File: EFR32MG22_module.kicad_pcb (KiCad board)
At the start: 2 copper layers, 29.9 x 42 mm, 34 parts, among them J1 USB_B_Micro 10118194-0011LF, J2 Conn_01x10, J3 Conn_ARM_JTAG_SWD_10, J4 Conn_01x10, U1 EFR32MG22C224F512GN32, U2 TLV75533PDBV, Y1 Crystal ECS-384-CDX-1983-TR3

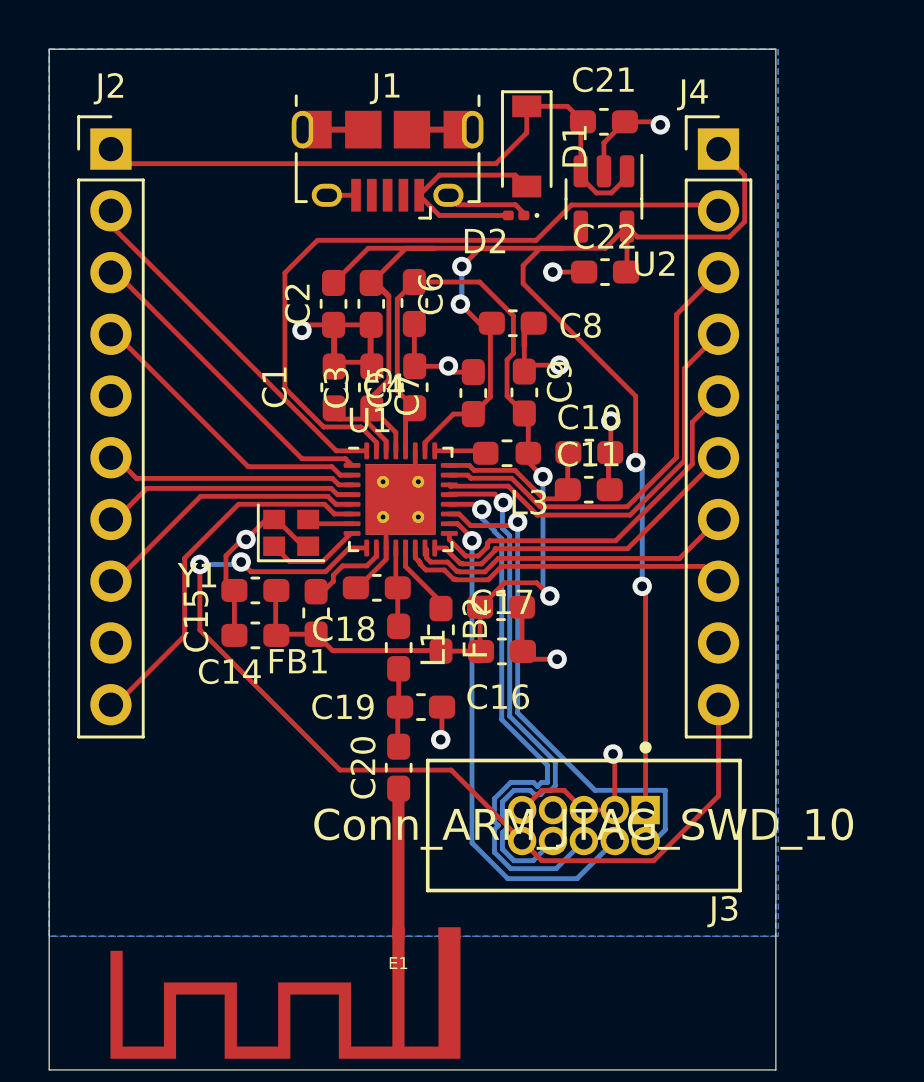
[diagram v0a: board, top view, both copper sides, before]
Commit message: better routing of ARM debug connector
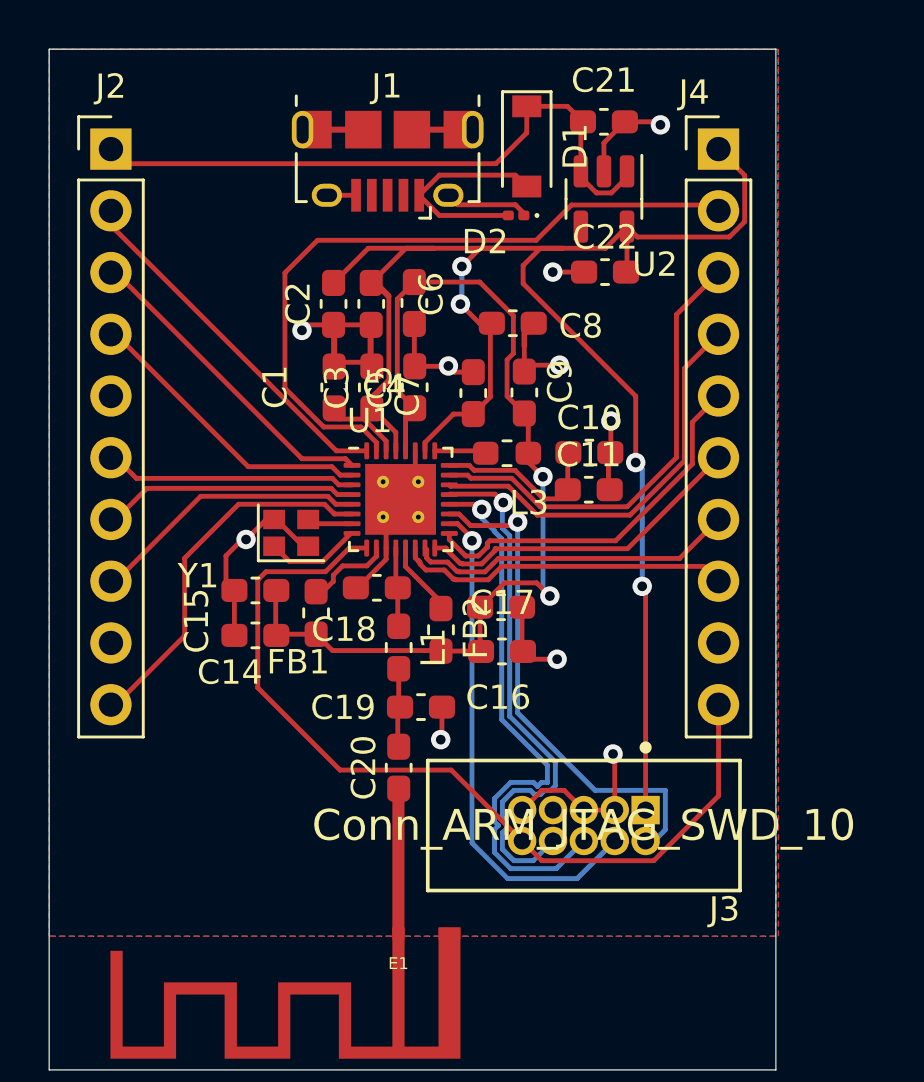
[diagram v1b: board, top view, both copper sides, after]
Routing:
- net /RESET_N: track 40.3 -> 36.2 mm, vias 2 -> 0
- added copper zone on F.Cu, net GND
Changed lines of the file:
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@@
     )
   )
-  (gr_rect (start 215 75) (end 245 125) (layer "F.Mask") (width 0.1) (fill none))
+  (gr_rect (start 215 80) (end 245 122) (layer "F.Mask") (width 0.1) (fill none))
   (gr_rect (start 215 80) (end 244.9 122) (layer "Edge.Cuts") (width 0.05) (fill none))
   (segment (start 234.18 86.4) (end 234.53 86.75) (width 0.2) (layer "F.Cu") (net 1))
@@
   (segment (start 233.682703 98.653949) (end 233.648 98.688652) (width 0.2) (layer "B.Cu") (net 27))
   (segment (start 233.648 112.913842) (end 234.123658 113.3895) (width 0.2) (layer "B.Cu") (net 27))
+  (segment (start 223.920598 101.5) (end 223.5805 101.840098) (width 0.2) (layer "F.Cu") (net 28))
   (segment (start 235.272 113.3895) (end 234.46 112.5775) (width 0.2) (layer "F.Cu") (net 28))
-  (segment (start 226.966098 109.6605) (end 221.2 103.894402) (width 0.2) (layer "F.Cu") (net 28))
+  (segment (start 223.5805 106.274902) (end 226.966098 109.6605) (width 0.2) (layer "F.Cu") (net 28))
   (segment (start 242.54 110.725842) (end 239.876342 113.3895) (width 0.2) (layer "F.Cu") (net 28))
   (segment (start 227.344742 100.525) (end 226.369742 101.5) (width 0.2) (layer "F.Cu") (net 28))
   (segment (start 231.543 109.6605) (end 226.966098 109.6605) (width 0.2) (layer "F.Cu") (net 28))
   (segment (start 242.54 106.97) (end 242.54 110.725842) (width 0.2) (layer "F.Cu") (net 28))
-  (segment (start 223.3 101.5) (end 226.369742 101.5) (width 0.2) (layer "F.Cu") (net 28))
   (segment (start 239.876342 113.3895) (end 235.272 113.3895) (width 0.2) (layer "F.Cu") (net 28))
   (segment (start 228.0625 100.525) (end 227.344742 100.525) (width 0.2) (layer "F.Cu") (net 28))
-  (segment (start 221.2 103.894402) (end 221.2 101.2) (width 0.2) (layer "F.Cu") (net 28))
-  (segment (start 223.3 101.5) (end 222.9 101.1) (width 0.2) (layer "F.Cu") (net 28))
+  (segment (start 226.369742 101.5) (end 223.920598 101.5) (width 0.2) (layer "F.Cu") (net 28))
+  (segment (start 223.5805 101.840098) (end 223.5805 106.274902) (width 0.2) (layer "F.Cu") (net 28))
   (segment (start 234.46 112.5775) (end 231.543 109.6605) (width 0.2) (layer "F.Cu") (net 28))
-  (via (at 222.9 101.1) (size 0.8) (drill 0.4) (layers "F.Cu" "B.Cu") (net 28))
-  (via (at 221.2 101.2) (size 0.8) (drill 0.4) (layers "F.Cu" "B.Cu") (net 28))
-  (segment (start 221.2 101.2) (end 222.8 101.2) (width 0.2) (layer "B.Cu") (net 28))
-  (segment (start 222.8 101.2) (end 222.9 101.1) (width 0.2) (layer "B.Cu") (net 28))
   (segment (start 226.918226 97.925) (end 226.653226 97.66) (width 0.2) (layer "F.Cu") (net 29))
   (segment (start 226.653226 97.66) (end 218.59 97.66) (width 0.2) (layer "F.Cu") (net 29))
@@
   (segment (start 239.4 102.1) (end 239.4 97.275009) (width 0.2) (layer "B.Cu") (net 38))
   (segment (start 231.98 90.43) (end 231.98 88.94) (width 0.2) (layer "B.Cu") (net 38))
-  (zone (net 1) (net_name "GND") (layer "B.Cu") (hatch edge 0.508)
+  (zone (net 1) (net_name "GND") (layer "F.Cu") (hatch edge 0.508)
     (connect_pads (clearance 0.508))
-    (min_thickness 0.254)
-    (fill (thermal_gap 0.508) (thermal_bridge_width 0.508))
+    (min_thickness 0.254) (filled_areas_thickness no)
+    (fill yes (thermal_gap 0.508) (thermal_bridge_width 0.508))
     (polygon
       (pts
+        (xy 215 116.5)
         (xy 245 116.5)
-        (xy 215 116.5)
+        (xy 245 80)
         (xy 215 80)
-        (xy 245 80)
       )
     )

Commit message: final commit? (?)
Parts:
- J3: value Conn_ARM_JTAG_SWD_10 -> ARM_2x5; footprint ARM_DEBUG:CNC_Tech_2x5_ARM_DEBUG -> arm_2x5:322010030000TR; moved to B.Cu
- L3: footprint Inductor_SMD:L_0603_1608Metric_Pad1.05x0.95mm_HandSolder -> Inductor_SMD:L_0805_2012Metric_Pad1.15x1.40mm_HandSolder
- moved C16 44.9 mm to (230.5, 149.5), turned to -90 degrees
- moved C17 44.3 mm to (229.7, 147.1), turned to 180 degrees
- moved D1 43.2 mm to (231.6, 127.1)
- moved D2 43.2 mm to (231.2, 129.9)
- moved C19 42.8 mm to (225.5, 149.6), turned to 180 degrees
- moved Y1 42.7 mm to (222.3, 142.5)
- moved L1 42.6 mm to (226.4, 147.1)
- moved C18 42.6 mm to (225.5, 144.7)
- moved C20 42.6 mm to (226.4, 152.1)
- moved C21 42.6 mm to (234.9, 125.5)
- moved C5 42.6 mm to (227.1, 136.4)
- moved C6 42.6 mm to (227.1, 133.0)
- moved J1 42.6 mm to (226.0, 127.1)
- moved J2 42.6 mm to (214.6, 126.6)
- moved J4 42.6 mm to (239.6, 126.6)
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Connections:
- J4 pad 10: /RESET_N -> GND
- J4 pad 9: GND -> /RESET_N
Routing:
- net VBUS: track 25.1 -> 48.1 mm
- net /DVDD: track 39.7 -> 62.7 mm, vias 2 -> 6
- net /TDI: track 22.2 -> 4.52 mm
- net /SWO: track 23.1 -> 6.89 mm
- net /SWDIO: track 20.7 -> 4.90 mm
- net /SWDCLK: track 20.8 -> 5.64 mm
- net +3.3V: track 75.5 -> 66.0 mm, vias 4 -> 3
- net GND: track 55.1 -> 45.7 mm, vias 10 -> 67
- net Net-(C20-Pad1): track 5.95 -> 1.31 mm
- net Net-(D1-Pad2): track 8.97 -> 5.55 mm
- net Net-(L3-Pad1): track 2.00 -> 4.93 mm
- net /RESET_N: track 36.2 -> 39.1 mm, vias 0 -> 3
- net /PA06: track 19.1 -> 16.3 mm
- net /PA05: track 16.9 -> 14.3 mm
- net /PAVDD: track 2.82 -> 3.90 mm
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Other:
- board size 29.9 x 42 mm -> 29.9 x 35.7 mm
- board text added: "3V3"
- board text added: "A moderately crappy Zigbee module"
- board text added: "A00"
- board text added: "A05"
- board text added: "A06"
- board text added: "B00"
- board text added: "B01"
- board text added: "D01"
- board text added: "GND"
- board text added: "PC00"
- board text added: "PC01"
- board text added: "PC02"
- board text added: "PC03"
- board text added: "PC04"
- board text added: "PC05"
- board text added: "PD00"
- board text added: "VBUS"
- board text added: "github.com/justchen1369"
- board text added: "{ "ViaStitching": "0.1", "stitch_zone_0": { "HSpacing": "1.27", "VSpacing": "1.27", "Clearance": "0.2", "Randomize": false }, "stitch_zone_1": { "HSpacing": "1", "VSpacing": "1", "Clearance": "0", "Randomize": false } }"

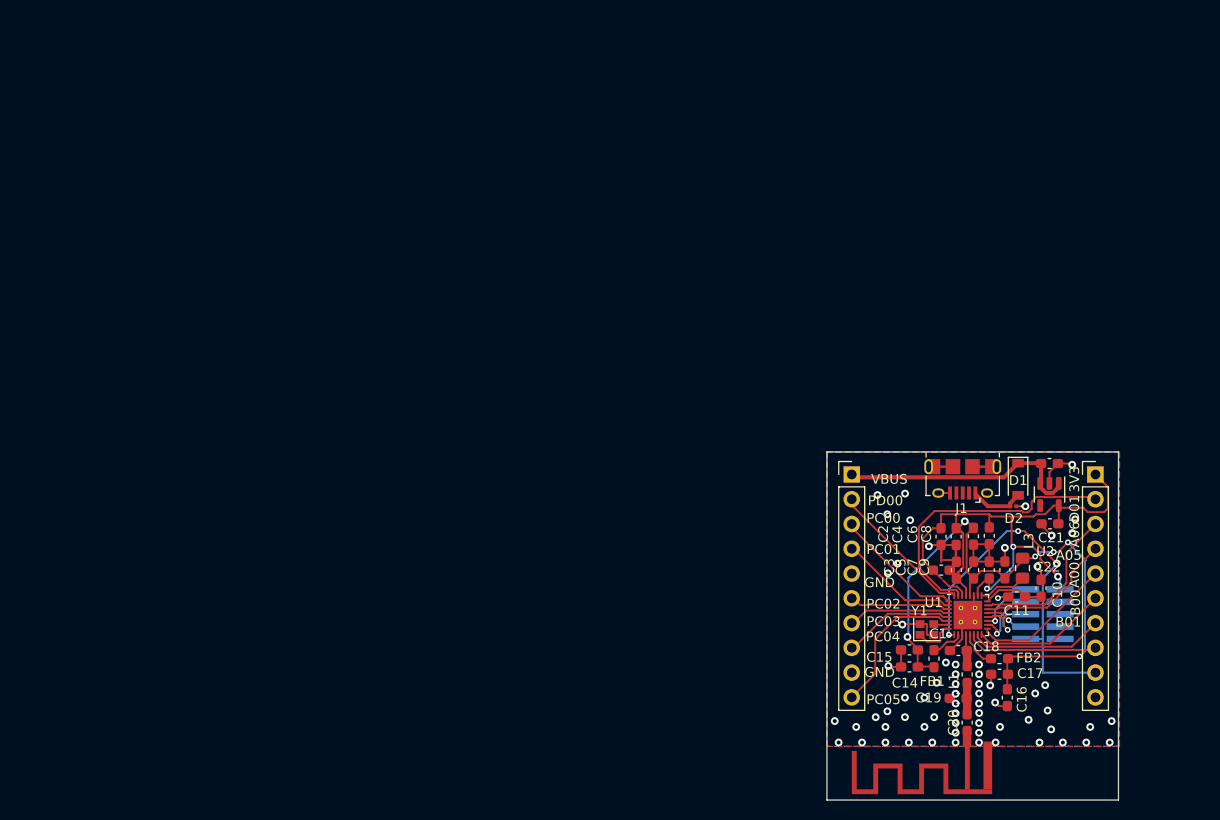
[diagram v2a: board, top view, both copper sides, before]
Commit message: first pass at layout and routing for second revision
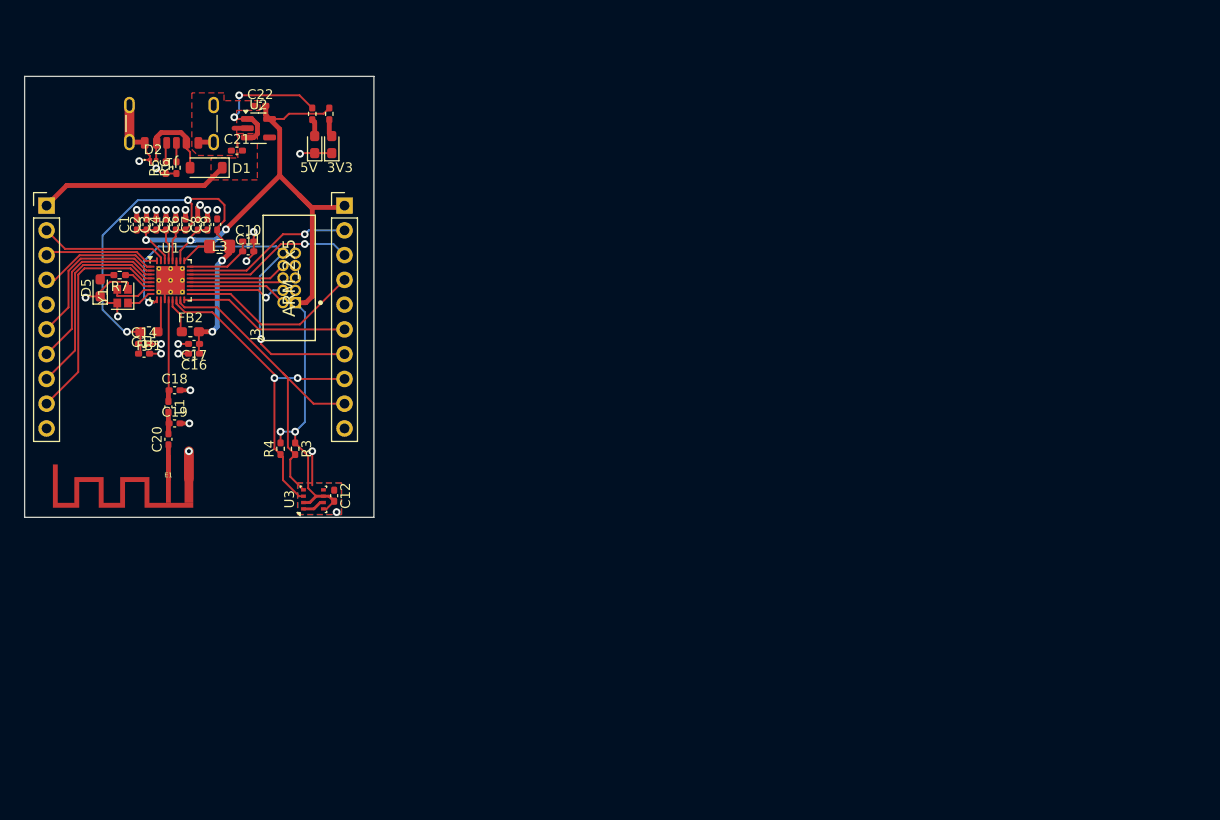
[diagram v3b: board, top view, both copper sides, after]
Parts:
- added C12: 0.1uF, Capacitor_SMD:C_0402_1005Metric_Pad0.74x0.62mm_HandSolder, F.Cu at (161.5, 128.8)
- added D3: LED, Diode_SMD:D_0603_1608Metric_Pad1.05x0.95mm_HandSolder, F.Cu at (159.5, 92.8)
- added D4: LED, Diode_SMD:D_0603_1608Metric_Pad1.05x0.95mm_HandSolder, F.Cu at (161.2, 92.8)
- added D5: LED, Diode_SMD:D_0603_1608Metric_Pad1.05x0.95mm_HandSolder, F.Cu at (137.5, 107.5)
- added R1: 4.7k, Resistor_SMD:R_0402_1005Metric_Pad0.72x0.64mm_HandSolder, F.Cu at (159.2, 89.7)
- added R2: 4.7k, Resistor_SMD:R_0402_1005Metric_Pad0.72x0.64mm_HandSolder, F.Cu at (161.0, 89.7)
- added R3: 4.7k, Resistor_SMD:R_0402_1005Metric_Pad0.72x0.64mm_HandSolder, F.Cu at (157.5, 124.0)
- added R4: 4.7k, Resistor_SMD:R_0402_1005Metric_Pad0.72x0.64mm_HandSolder, F.Cu at (156.0, 124.0)
- added R5: 5.1k, Resistor_SMD:R_0402_1005Metric_Pad0.72x0.64mm_HandSolder, F.Cu at (144.2, 95.2)
- added R6: 5.1k, Resistor_SMD:R_0402_1005Metric_Pad0.72x0.64mm_HandSolder, F.Cu at (145.3, 95.2)
- added R7: 4.7k, Resistor_SMD:R_0402_1005Metric_Pad0.72x0.64mm_HandSolder, F.Cu at (139.5, 106.2)
- added U3: BME280, Package_LGA:Bosch_LGA-8_2.5x2.5mm_P0.65mm_ClockwisePinNumbering, F.Cu at (159.4, 129.2)
- C1, C10, C11, C14, C16, C17, C18, C19, C2, C20, C21, C22, C3, C4, C5, C6, C7, C8, C9: footprint Capacitor_SMD:C_0603_1608Metric_Pad1.08x0.95mm_HandSolder -> Capacitor_SMD:C_0402_1005Metric_Pad0.74x0.62mm_HandSolder
- C15: value 100nF -> 0.1uF; footprint Capacitor_SMD:C_0603_1608Metric_Pad1.08x0.95mm_HandSolder -> Capacitor_SMD:C_0402_1005Metric_Pad0.74x0.62mm_HandSolder
- J1: value USB_B_Micro 10118194-0011LF -> USB_C_Receptacle_PowerOnly_6P; footprint Connector_USB:USB_Micro-B_Amphenol_10118194_Horizontal -> Connector_USB:USB_C_Receptacle_GCT_USB4125-xx-x-0190_6P_TopMnt_Horizontal
- J3: footprint arm_2x5:322010030000TR -> ARM_DEBUG:CNC_Tech_2x5_ARM_DEBUG; moved to F.Cu
- L1: footprint Inductor_SMD:L_0603_1608Metric_Pad1.05x0.95mm_HandSolder -> Inductor_SMD:L_0402_1005Metric_Pad0.77x0.64mm_HandSolder
- moved D2 95.1 mm to (142.9, 94.4), turned to 0 degrees
- moved C22 91.6 mm to (153.9, 88.8)
- moved C16 90.6 mm to (147.1, 114.2), turned to 180 degrees
- moved C1 89.8 mm to (141.2, 101.0), turned to 90 degrees
- moved FB2 89.5 mm to (146.8, 112.0)
- moved J1 89.4 mm to (144.8, 89.5)
- moved U2 89.4 mm to (153.7, 91.1), turned to 0 degrees
- moved C3 89.4 mm to (143.2, 101.0)
- moved C21 89.3 mm to (151.5, 93.4), turned to 0 degrees
- moved C17 89.3 mm to (147.1, 113.2)
- moved Y1 89.3 mm to (139.8, 108.3), turned to 90 degrees
- moved D1 89.2 mm to (148.4, 95.2), turned to 180 degrees
- moved C5 89.2 mm to (145.2, 101.0)
- moved C10 88.7 mm to (152.7, 102.8), turned to 0 degrees
- moved L3 88.7 mm to (149.8, 103.2), turned to 0 degrees
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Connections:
- net /PB02 renamed /SDA
- D1 pad 2: Net-(D1-Pad2) -> Net-(D1-A)
- D2 pad 2: Net-(D1-Pad2) -> Net-(D1-A)
- J2 pad 10: /PC05 -> GND
- J2 pad 2: /PD00 -> /PD01
- J2 pad 3: /PC00 -> /PD00
- J2 pad 4: /PC01 -> /PC00
- J2 pad 6: /PC02 -> /PC01
- J2 pad 7: /PC03 -> /PC02
- J2 pad 8: /PC04 -> /PC03
- J2 pad 9: GND -> /PC04
- J4 pad 2: /PD01 -> /PA06
- J4 pad 3: /PA06 -> /PA05
- J4 pad 4: /PA05 -> /PA00
- J4 pad 5: /PA00 -> GND
- J4 pad 7: /PB01 -> /RESET_N
- J4 pad 9: /RESET_N -> /SCL
- U1 pad 15: /PB01 -> /SCL
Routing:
- net /SCL: track 0.00 -> 34.7 mm
- net +3.3V: track 66.0 -> 96.5 mm, vias 3 -> 5
- net /SDA: track 13.2 -> 34.7 mm, vias 0 -> 2
- net /PD01: track 29.3 -> 13.2 mm
- net /PB01: track 13.8 -> 0.00 mm
- net VBUS: track 48.1 -> 35.0 mm, vias 0 -> 2
- net /PC05: track 15.6 -> 3.10 mm
- net /PC04: track 11.3 -> 22.9 mm
- net GND: track 45.7 -> 56.1 mm, vias 67 -> 25
- net /PC03: track 10.4 -> 20.8 mm
- net Net-(D1-A): track 0.00 -> 8.95 mm
- net /PC02: track 10.2 -> 18.6 mm
- net /DVDD: track 62.7 -> 54.6 mm, vias 6 -> 4
- net /RF2G4_IO: track 3.10 -> 10.1 mm
- net Net-(D1-Pad2): track 5.55 -> 0.00 mm
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- added copper zone on In1.Cu, net GND
- added copper zone on In2.Cu, net GND
- added copper zone on F.Cu, net VBUS
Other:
- board size 29.9 x 35.7 mm -> 35.8 x 45.2 mm
- copper layers 2 -> 4
- board text added: "5V"
- board text removed: "A moderately crappy Zigbee module"
- board text removed: "A00"
- board text removed: "A05"
- board text removed: "A06"
- board text removed: "B00"
- board text removed: "B01"
- board text removed: "D01"
- board text removed: "GND"
- board text removed: "PC00"
- board text removed: "PC01"
- board text removed: "PC02"
- board text removed: "PC03"
- board text removed: "PC04"
- board text removed: "PC05"
- board text removed: "PD00"
- board text removed: "VBUS"
- board text removed: "github.com/justchen1369"
